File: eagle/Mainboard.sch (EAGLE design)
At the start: 29 parts, among them IC1 L293D, IC2 TLC272P, IC3 LM1085IT-5.0

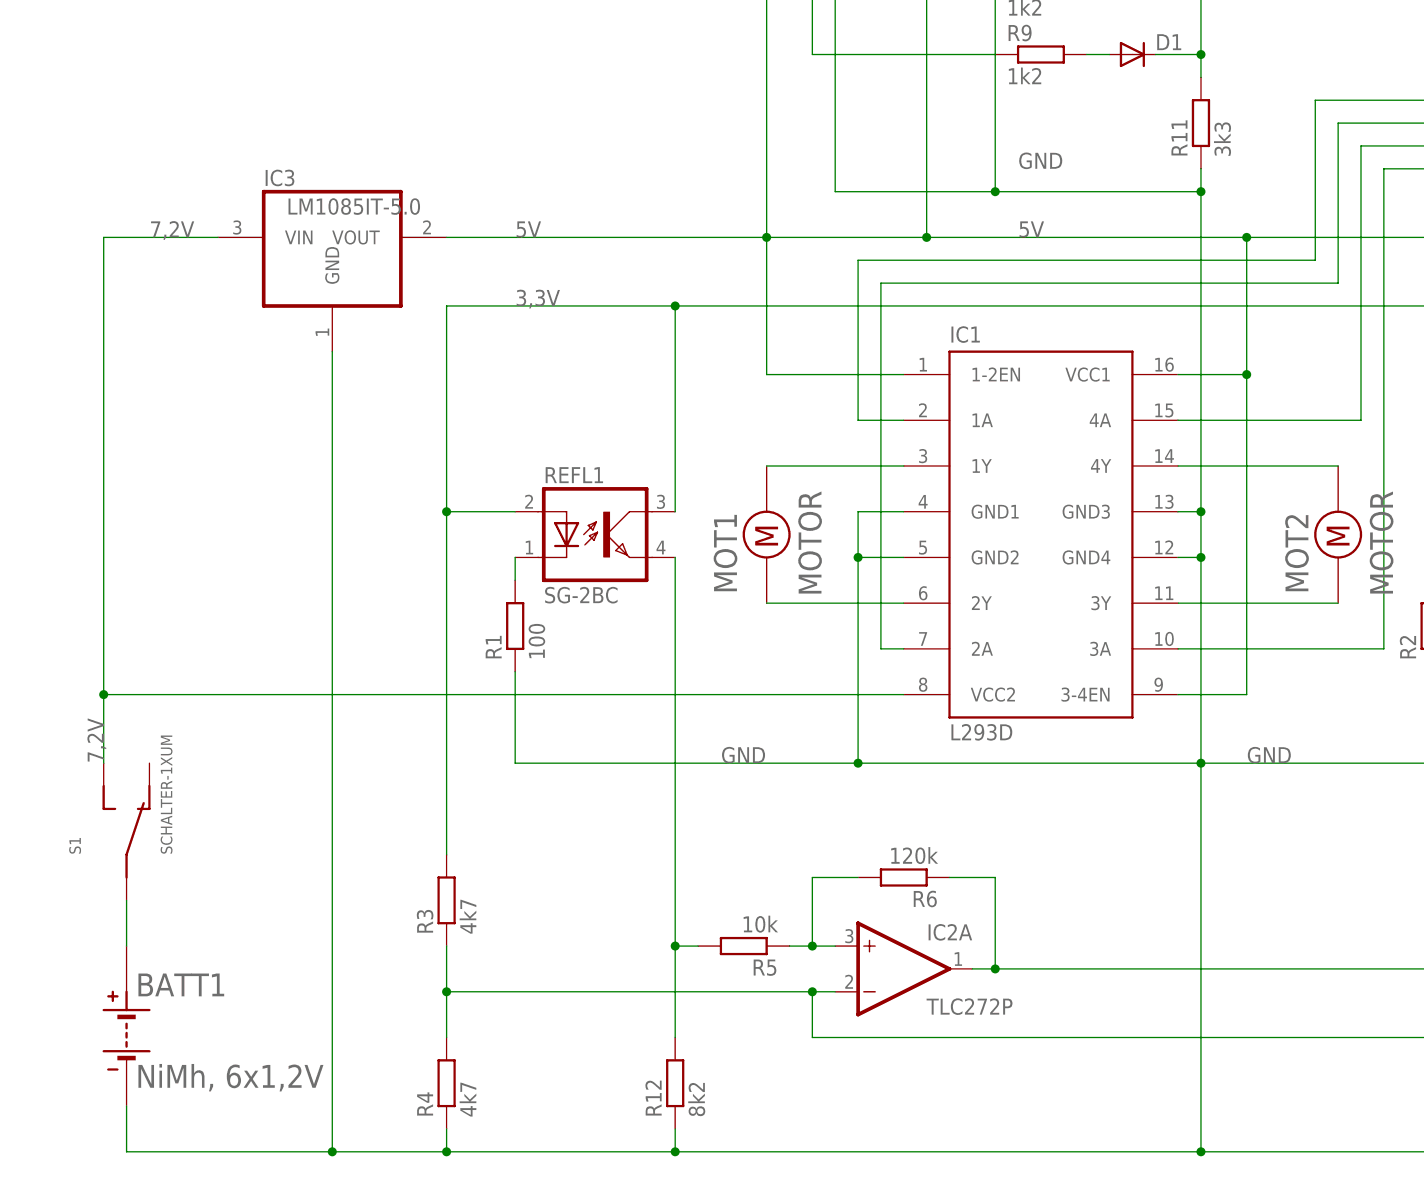
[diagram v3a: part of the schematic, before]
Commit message: Kondensatoren um Spannungsregler hinzugefügt
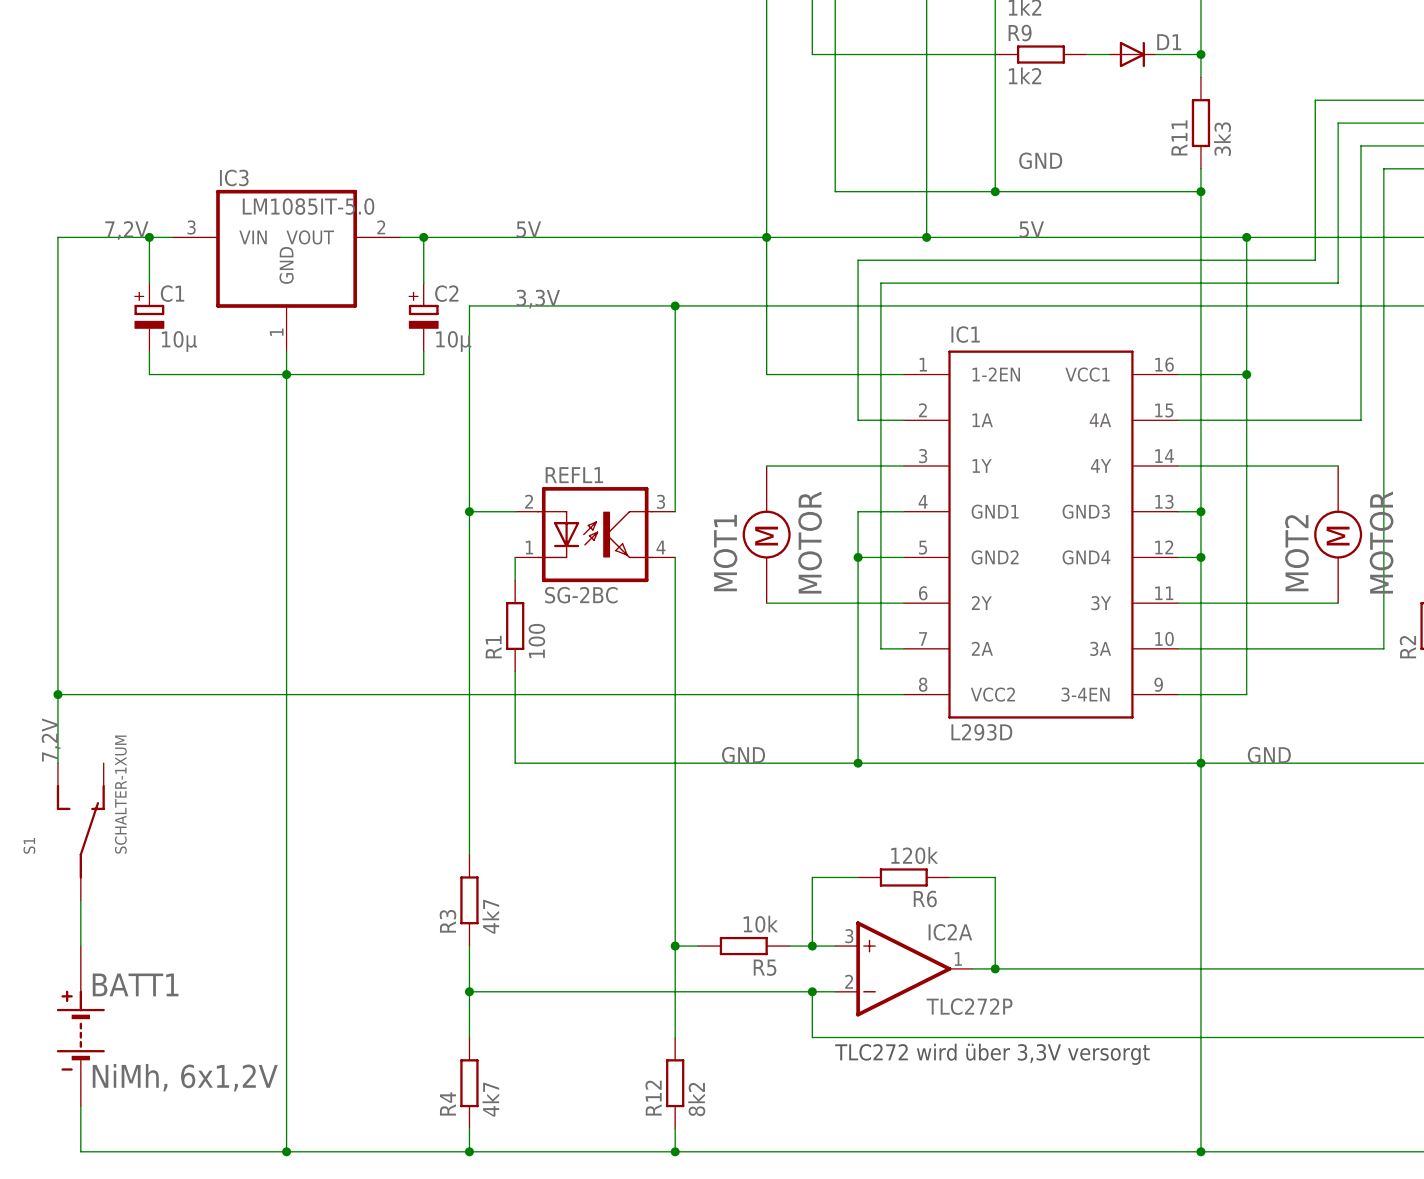
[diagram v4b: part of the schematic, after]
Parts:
- added C1, C2: 10µ, rcl:CPOL-EUE3.5-10
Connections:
- net 5V: now also C2.+
- net 7,2V: now also C1.+
- net GND: now also C1.-, C2.-
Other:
- note added: "TLC272 wird über 3,3V versorgt"
- moved on the sheet: BATT1, IC3, R3, R4, S1
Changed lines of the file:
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@@
 <part name="R12" library="rcl" library_urn="urn:adsk.eagle:library:334" deviceset="R-EU_" device="RDH/15" package3d_urn="urn:adsk.eagle:package:23595/1" value="8k2"/>
 <part name="R13" library="rcl" library_urn="urn:adsk.eagle:library:334" deviceset="R-EU_" device="RDH/15" package3d_urn="urn:adsk.eagle:package:23595/1" value="8k2"/>
+<part name="C1" library="rcl" library_urn="urn:adsk.eagle:library:334" deviceset="CPOL-EU" device="E3.5-10" package3d_urn="urn:adsk.eagle:package:23351/1" value="10µ"/>
+<part name="C2" library="rcl" library_urn="urn:adsk.eagle:library:334" deviceset="CPOL-EU" device="E3.5-10" package3d_urn="urn:adsk.eagle:package:23351/1" value="10µ"/>
 </parts>
 <sheets>
@@
 <text x="220.98" y="132.08" size="1.778" layer="95">RST</text>
 <text x="220.98" y="129.54" size="1.778" layer="95">BL</text>
+<text x="81.28" y="15.24" size="1.778" layer="97">TLC272 wird über 3,3V versorgt</text>
 </plain>
 <instances>
-<instance part="BATT1" gate="G$1" x="2.54" y="20.32"/>
+<instance part="BATT1" gate="G$1" x="-2.54" y="20.32"/>
 <instance part="IC1" gate="G$1" x="104.14" y="73.66"/>
 <instance part="REFL1" gate="G$1" x="55.88" y="73.66"/>
@@
 <instance part="MOT1" gate="G$1" x="73.66" y="73.66" rot="R90"/>
 <instance part="MOT2" gate="G$1" x="137.16" y="73.66" rot="R90"/>
-<instance part="S1" gate="G$1" x="2.54" y="40.64" rot="R90"/>
-<instance part="IC3" gate="G$1" x="25.4" y="106.68"/>
+<instance part="S1" gate="G$1" x="-2.54" y="40.64" rot="R90"/>
+<instance part="IC3" gate="G$1" x="20.32" y="106.68"/>
 <instance part="R1" gate="G$1" x="45.72" y="63.5" rot="R90"/>
 <instance part="R2" gate="G$1" x="147.32" y="63.5" rot="R90"/>
@@
 <instance part="US1" gate="A" x="78.74" y="152.4" rot="R90"/>
 <instance part="US2" gate="A" x="96.52" y="152.4" rot="R90"/>
-<instance part="R3" gate="G$1" x="38.1" y="33.02" rot="R90"/>
-<instance part="R4" gate="G$1" x="38.1" y="12.7" rot="R90"/>
+<instance part="R3" gate="G$1" x="40.64" y="33.02" rot="R90"/>
+<instance part="R4" gate="G$1" x="40.64" y="12.7" rot="R90"/>
 <instance part="R5" gate="G$1" x="71.12" y="27.94" rot="R180"/>
 <instance part="R6" gate="G$1" x="88.9" y="35.56" rot="R180"/>
@@
 <instance part="R12" gate="G$1" x="63.5" y="12.7" rot="R90"/>
 <instance part="R13" gate="G$1" x="167.64" y="12.7" rot="R90"/>
+<instance part="C1" gate="G$1" x="5.08" y="99.06"/>
+<instance part="C2" gate="G$1" x="35.56" y="99.06"/>
 </instances>
 <busses>
@@
 <pinref part="BATT1" gate="G$1" pin="P"/>
 <pinref part="S1" gate="G$1" pin="P$1"/>
-<wire x1="2.54" y1="27.94" x2="2.54" y2="33.02" width="0.1524" layer="91"/>
+<wire x1="-2.54" y1="27.94" x2="-2.54" y2="33.02" width="0.1524" layer="91"/>
 </segment>
 </net>
@@
 <segment>
 <pinref part="BATT1" gate="G$1" pin="M"/>
-<wire x1="2.54" y1="5.08" x2="2.54" y2="10.16" width="0.1524" layer="91"/>
+<wire x1="-2.54" y1="5.08" x2="-2.54" y2="10.16" width="0.1524" layer="91"/>
 <wire x1="121.92" y1="5.08" x2="63.5" y2="5.08" width="0.1524" layer="91"/>
-<wire x1="63.5" y1="5.08" x2="38.1" y2="5.08" width="0.1524" layer="91"/>
-<wire x1="38.1" y1="5.08" x2="25.4" y2="5.08" width="0.1524" layer="91"/>
-<wire x1="25.4" y1="5.08" x2="2.54" y2="5.08" width="0.1524" layer="91"/>
+<wire x1="63.5" y1="5.08" x2="40.64" y2="5.08" width="0.1524" layer="91"/>
+<wire x1="40.64" y1="5.08" x2="20.32" y2="5.08" width="0.1524" layer="91"/>
+<wire x1="20.32" y1="5.08" x2="-2.54" y2="5.08" width="0.1524" layer="91"/>
 <pinref part="IC1" gate="G$1" pin="GND3"/>
 <wire x1="119.38" y1="76.2" x2="121.92" y2="76.2" width="0.1524" layer="91"/>
@@
 <pinref part="IC3" gate="G$1" pin="GND"/>
 <wire x1="167.64" y1="5.08" x2="208.28" y2="5.08" width="0.1524" layer="91"/>
-<wire x1="25.4" y1="93.98" x2="25.4" y2="5.08" width="0.1524" layer="91"/>
-<junction x="25.4" y="5.08"/>
+<wire x1="20.32" y1="93.98" x2="20.32" y2="91.44" width="0.1524" layer="91"/>
+<junction x="20.32" y="5.08"/>
 <pinref part="IC1" gate="G$1" pin="GND2"/>
 <pinref part="IC1" gate="G$1" pin="GND1"/>
+<wire x1="20.32" y1="91.44" x2="20.32" y2="5.08" width="0.1524" layer="91"/>
 <wire x1="88.9" y1="76.2" x2="83.82" y2="76.2" width="0.1524" layer="91"/>
 <wire x1="83.82" y1="76.2" x2="83.82" y2="71.12" width="0.1524" layer="91"/>
@@
 <junction x="121.92" y="48.26"/>
 <pinref part="R4" gate="G$1" pin="1"/>
-<wire x1="38.1" y1="7.62" x2="38.1" y2="5.08" width="0.1524" layer="91"/>
-<junction x="38.1" y="5.08"/>
+<wire x1="40.64" y1="7.62" x2="40.64" y2="5.08" width="0.1524" layer="91"/>
+<junction x="40.64" y="5.08"/>
 <pinref part="R1" gate="G$1" pin="1"/>
 <wire x1="45.72" y1="58.42" x2="45.72" y2="48.26" width="0.1524" layer="91"/>
@@
 <wire x1="167.64" y1="5.08" x2="167.64" y2="7.62" width="0.1524" layer="91"/>
 <junction x="167.64" y="5.08"/>
+<pinref part="C1" gate="G$1" pin="-"/>
+<wire x1="5.08" y1="93.98" x2="5.08" y2="91.44" width="0.1524" layer="91"/>
+<wire x1="5.08" y1="91.44" x2="20.32" y2="91.44" width="0.1524" layer="91"/>
+<junction x="20.32" y="91.44"/>
+<pinref part="C2" gate="G$1" pin="-"/>
+<wire x1="20.32" y1="91.44" x2="35.56" y2="91.44" width="0.1524" layer="91"/>
+<wire x1="35.56" y1="91.44" x2="35.56" y2="93.98" width="0.1524" layer="91"/>
 </segment>
 </net>
@@
 <wire x1="119.38" y1="55.88" x2="127" y2="55.88" width="0.1524" layer="91"/>
 <pinref part="IC3" gate="G$1" pin="VOUT"/>
-<wire x1="38.1" y1="106.68" x2="73.66" y2="106.68" width="0.1524" layer="91"/>
+<wire x1="33.02" y1="106.68" x2="35.56" y2="106.68" width="0.1524" layer="91"/>
+<wire x1="35.56" y1="106.68" x2="73.66" y2="106.68" width="0.1524" layer="91"/>
 <wire x1="73.66" y1="106.68" x2="91.44" y2="106.68" width="0.1524" layer="91"/>
 <pinref part="SV1" gate="G$1" pin="20"/>
@@
 <wire x1="73.66" y1="106.68" x2="73.66" y2="91.44" width="0.1524" layer="91"/>
 <label x="45.72" y="106.68" size="1.778" layer="95"/>
+<pinref part="C2" gate="G$1" pin="+"/>
+<wire x1="35.56" y1="101.6" x2="35.56" y2="106.68" width="0.1524" layer="91"/>
+<junction x="35.56" y="106.68"/>
 </segment>
 </net>
@@
 <pinref part="R4" gate="G$1" pin="2"/>
 <pinref part="IC2" gate="A" pin="-IN"/>
-<wire x1="38.1" y1="22.86" x2="38.1" y2="17.78" width="0.1524" layer="91"/>
-<wire x1="38.1" y1="22.86" x2="78.74" y2="22.86" width="0.1524" layer="91"/>
+<wire x1="40.64" y1="22.86" x2="40.64" y2="17.78" width="0.1524" layer="91"/>
+<wire x1="40.64" y1="22.86" x2="78.74" y2="22.86" width="0.1524" layer="91"/>
 <wire x1="78.74" y1="22.86" x2="81.28" y2="22.86" width="0.1524" layer="91"/>
 <wire x1="78.74" y1="22.86" x2="78.74" y2="17.78" width="0.1524" layer="91"/>
@@
 <wire x1="162.56" y1="22.86" x2="182.88" y2="22.86" width="0.1524" layer="91"/>
 <pinref part="R3" gate="G$1" pin="1"/>
-<wire x1="38.1" y1="27.94" x2="38.1" y2="22.86" width="0.1524" layer="91"/>
-<junction x="38.1" y="22.86"/>
+<wire x1="40.64" y1="27.94" x2="40.64" y2="22.86" width="0.1524" layer="91"/>
+<junction x="40.64" y="22.86"/>
 </segment>
 </net>
@@
 <pinref part="REFL1" gate="G$1" pin="COL"/>
 <wire x1="63.5" y1="99.06" x2="63.5" y2="76.2" width="0.1524" layer="91"/>
-<wire x1="38.1" y1="99.06" x2="63.5" y2="99.06" width="0.1524" layer="91"/>
-<pinref part="REFL1" gate="G$1" pin="A"/>
-<wire x1="45.72" y1="76.2" x2="38.1" y2="76.2" width="0.1524" layer="91"/>
-<wire x1="38.1" y1="76.2" x2="38.1" y2="99.06" width="0.1524" layer="91"/>
+<wire x1="40.64" y1="99.06" x2="63.5" y2="99.06" width="0.1524" layer="91"/>
 <wire x1="147.32" y1="99.06" x2="63.5" y2="99.06" width="0.1524" layer="91"/>
 <junction x="147.32" y="99.06"/>
@@
 <label x="45.72" y="99.06" size="1.778" layer="95"/>
 <pinref part="R3" gate="G$1" pin="2"/>
-<wire x1="38.1" y1="76.2" x2="38.1" y2="38.1" width="0.1524" layer="91"/>
-<junction x="38.1" y="76.2"/>
+<pinref part="REFL1" gate="G$1" pin="A"/>
+<wire x1="45.72" y1="76.2" x2="40.64" y2="76.2" width="0.1524" layer="91"/>
+<wire x1="40.64" y1="76.2" x2="40.64" y2="38.1" width="0.1524" layer="91"/>
+<wire x1="40.64" y1="99.06" x2="40.64" y2="76.2" width="0.1524" layer="91"/>
+<junction x="40.64" y="76.2"/>
 </segment>
 </net>
@@
 <segment>
 <pinref part="IC1" gate="G$1" pin="VCC2"/>
-<wire x1="88.9" y1="55.88" x2="0" y2="55.88" width="0.1524" layer="91"/>
+<wire x1="88.9" y1="55.88" x2="-5.08" y2="55.88" width="0.1524" layer="91"/>
 <pinref part="IC3" gate="G$1" pin="VIN"/>
 <pinref part="S1" gate="G$1" pin="P$2"/>
-<wire x1="0" y1="48.26" x2="0" y2="55.88" width="0.1524" layer="91"/>
-<wire x1="0" y1="55.88" x2="0" y2="106.68" width="0.1524" layer="91"/>
-<wire x1="0" y1="106.68" x2="12.7" y2="106.68" width="0.1524" layer="91"/>
-<junction x="0" y="55.88"/>
-<label x="0" y="48.26" size="1.778" layer="95" rot="R90"/>
-<label x="5.08" y="106.68" size="1.778" layer="95"/>
-</segment>
-</net>
+<wire x1="-5.08" y1="48.26" x2="-5.08" y2="55.88" width="0.1524" layer="91"/>
+<wire x1="-5.08" y1="55.88" x2="-5.08" y2="106.68" width="0.1524" layer="91"/>
+<wire x1="-5.08" y1="106.68" x2="5.08" y2="106.68" width="0.1524" layer="91"/>
+<junction x="-5.08" y="55.88"/>
+<label x="-5.08" y="48.26" size="1.778" layer="95" rot="R90"/>
+<label x="0" y="106.68" size="1.778" layer="95"/>
+<pinref part="C1" gate="G$1" pin="+"/>
+<wire x1="5.08" y1="106.68" x2="7.62" y2="106.68" width="0.1524" layer="91"/>
+<wire x1="5.08" y1="106.68" x2="5.08" y2="101.6" width="0.1524" layer="91"/>
+<junction x="5.08" y="106.68"/>
+</segment>
+</net>
